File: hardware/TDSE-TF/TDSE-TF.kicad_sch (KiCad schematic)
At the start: 27 parts, among them J1 Sensor nivel de agua, J10 CN10, J2 Tira LED, J3 +5VCC entrada, J5 Bomba, J6 Sensor nivel de luz, J7 CN7, J8 Sensor humedad de suelo, J9 Conector LCD16x02, Q1 IRLZ44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

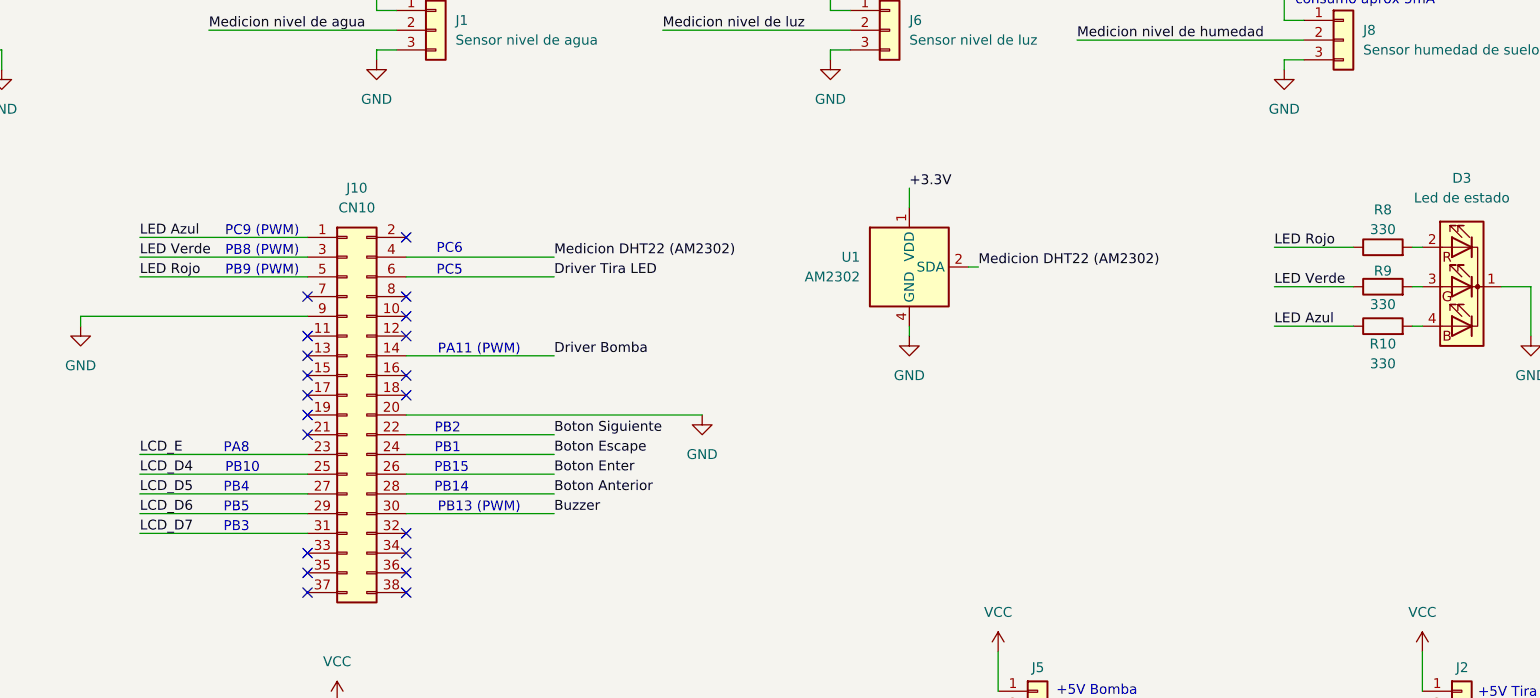
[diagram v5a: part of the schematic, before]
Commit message: PCB final Rev 3
Mejorados detalles del PCB y serigrafía
Añadida opcion de agregar un pullup para el dht22
Modificado el .ioc
Creado task_state_led.h (no terminado)
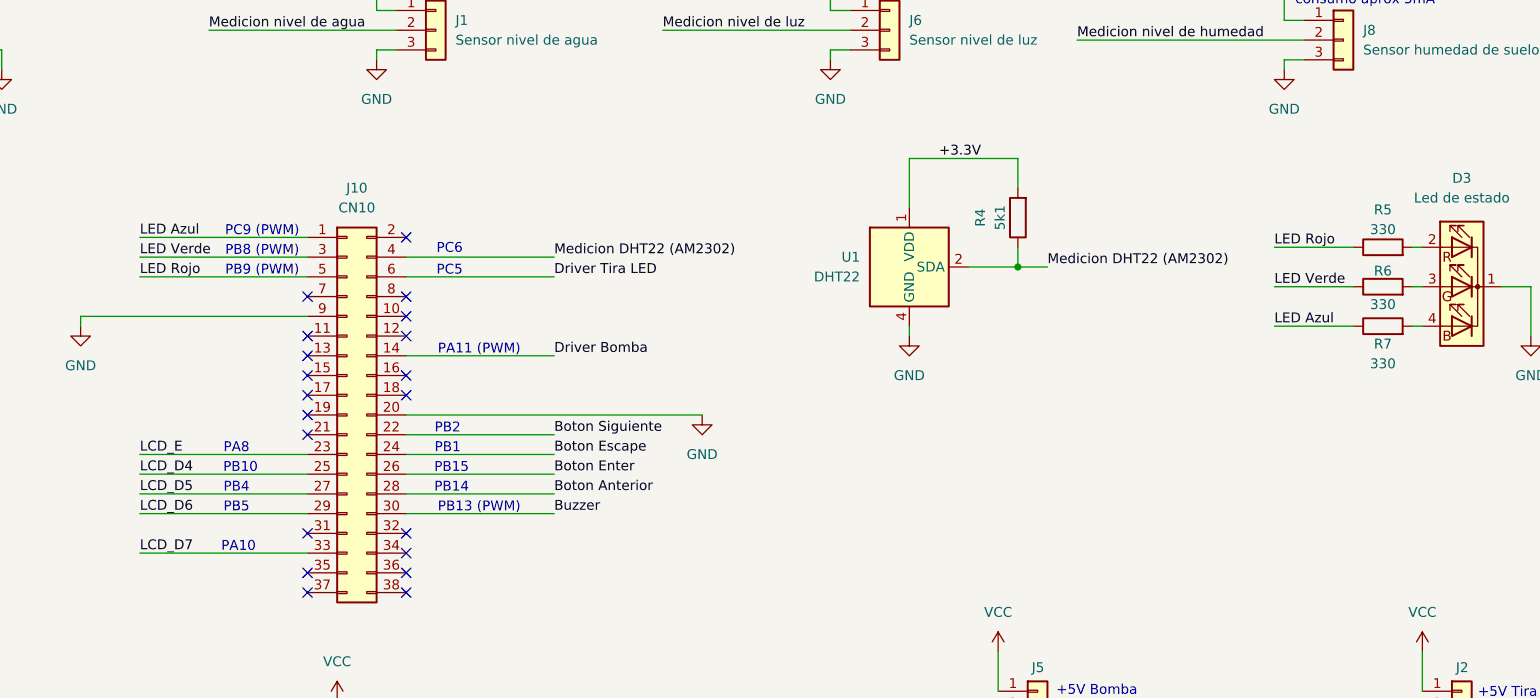
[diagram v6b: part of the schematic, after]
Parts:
- added R4: 5k1, Resistor_THT:R_Axial_DIN0207_L6.3mm_D2.5mm_P7.62mm_Horizontal, symbol Device:R
- U1: value AM2302 -> DHT22
- renumbered R8 to R5, R9 to R6, R10 to R7
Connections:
- net +3.3V: now also R4.2
- net LCD_D7: now also J10.33 (Pin_33); no longer J10.31 (Pin_31)
- net Medicion DHT22 (AM2302): now also R4.1
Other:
- note added: "PA10"
- note removed: "PB3"
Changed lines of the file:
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@@
 		)
 	)
-	(text "PB3"
+	(text "PA10"
 		(exclude_from_sim no)
-		(at 108.966 93.218 0)
+		(at 109.22 95.758 0)
 		(effects
 			(font
@@
 	(text "PB10"
 		(exclude_from_sim no)
-		(at 109.728 85.598 0)
+		(at 109.474 85.598 0)
 		(effects
 			(font
@@
 	)
 	(junction
+		(at 209.55 59.69)
+		(diameter 0)
+		(color 0 0 0 0)
+	)
+	(junction
 		(at 247.65 137.16)
 		(diameter 0)
@@
 	)
 	(no_connect
-		(at 118.11 96.52)
+		(at 118.11 93.98)
 	)
 	(no_connect
@@
 	(wire
 		(pts
+			(xy 209.55 45.72) (xy 195.58 45.72)
+		)
+		(stroke
+			(width 0)
+			(type default)
+		)
+	)
+	(wire
+		(pts
 			(xy 96.52 58.42) (xy 118.11 58.42)
 		)
@@
 	(wire
 		(pts
+			(xy 209.55 57.15) (xy 209.55 59.69)
+		)
+		(stroke
+			(width 0)
+			(type default)
+		)
+	)
+	(wire
+		(pts
 			(xy 191.77 137.16) (xy 191.77 139.7)
 		)
@@
 	(wire
 		(pts
-			(xy 203.2 59.69) (xy 204.47 59.69)
+			(xy 203.2 59.69) (xy 209.55 59.69)
 		)
 		(stroke
@@
 	(wire
 		(pts
+			(xy 209.55 49.53) (xy 209.55 45.72)
+		)
+		(stroke
+			(width 0)
+			(type default)
+		)
+	)
+	(wire
+		(pts
 			(xy 93.98 149.86) (xy 93.98 152.4)
 		)
@@
 	(wire
 		(pts
+			(xy 209.55 59.69) (xy 213.36 59.69)
+		)
+		(stroke
+			(width 0)
+			(type default)
+		)
+	)
+	(wire
+		(pts
 			(xy 137.16 151.13) (xy 146.05 151.13)
 		)
@@
 	(wire
 		(pts
+			(xy 195.58 45.72) (xy 195.58 52.07)
+		)
+		(stroke
+			(width 0)
+			(type default)
+		)
+	)
+	(wire
+		(pts
 			(xy 62.23 181.61) (xy 83.82 181.61)
 		)
@@
 	(wire
 		(pts
-			(xy 195.58 49.53) (xy 195.58 52.07)
-		)
-		(stroke
-			(width 0)
-			(type default)
-		)
-	)
-	(wire
-		(pts
 			(xy 163.83 29.21) (xy 187.96 29.21)
 		)
@@
 	(wire
 		(pts
-			(xy 96.52 93.98) (xy 118.11 93.98)
+			(xy 96.52 96.52) (xy 118.11 96.52)
 		)
 		(stroke
@@
 	)
 	(label "Medicion DHT22 (AM2302)"
-		(at 204.47 59.69 0)
+		(at 213.36 59.69 0)
 		(effects
 			(font
@@
 	)
 	(label "+3.3V"
-		(at 195.58 49.53 0)
+		(at 199.39 45.72 0)
 		(effects
 			(font
@@
 	)
 	(label "LCD_D7"
-		(at 96.52 93.98 0)
+		(at 96.52 96.52 0)
 		(effects
 			(font
@@
 	)
 	(symbol
+		(lib_id "Device:R")
+		(at 209.55 53.34 180)
+		(unit 1)
+		(body_style 1)
+		(exclude_from_sim no)
+		(in_bom yes)
+		(on_board yes)
+		(in_pos_files yes)
+		(dnp no)
+		(property "Reference" "R4"
+			(at 204.724 53.34 90)
+			(show_name no)
+			(do_not_autoplace no)
+			(effects
+				(font
+					(size 1.27 1.27)
+				)
+			)
+		)
+		(property "Value" "5k1"
+			(at 207.264 53.34 90)
+			(show_name no)
+			(do_not_autoplace no)
+			(effects
+				(font
+					(size 1.27 1.27)
+				)
+			)
+		)
+		(property "Footprint" "Resistor_THT:R_Axial_DIN0207_L6.3mm_D2.5mm_P7.62mm_Horizontal"
+			(at 211.328 53.34 90)
+			(hide yes)
+			(show_name no)
+			(do_not_autoplace no)
+			(effects
+				(font
+					(size 1.27 1.27)
+				)
+			)
+		)
+		(property "Datasheet" ""
+			(at 209.55 53.34 0)
+			(hide yes)
+			(show_name no)
+			(do_not_autoplace no)
+			(effects
+				(font
+					(size 1.27 1.27)
+				)
+			)
+		)
+		(property "Description" "Resistor"
+			(at 209.55 53.34 0)
+			(hide yes)
+			(show_name no)
+			(do_not_autoplace no)
+			(effects
+				(font
+					(size 1.27 1.27)
+				)
+			)
+		)
+		(pin "2"
+		)
+		(pin "1"
+		)
+		(instances
+			(project "TDSE-TF"
+				(path "/f326f9a1-cd10-4b99-adfe-c3556115ef97"
+					(reference "R4")
+					(unit 1)
+				)
+			)
+		)
+	)
+	(symbol
 		(lib_id "Connector_Generic:Conn_02x19_Odd_Even")
 		(at 34.29 78.74 0)
@@
 		(in_pos_files yes)
 		(dnp no)
-		(property "Reference" "R8"
+		(property "Reference" "R5"
 			(at 256.54 52.324 90)
 			(show_name no)
@@
 			(project "TDSE-TF"
 				(path "/f326f9a1-cd10-4b99-adfe-c3556115ef97"
-					(reference "R8")
+					(reference "R5")
 					(unit 1)
 				)
@@
 		(in_pos_files yes)
 		(dnp no)
-		(property "Reference" "R9"
+		(property "Reference" "R6"
 			(at 256.54 60.198 90)
 			(show_name no)
@@
 			(project "TDSE-TF"
 				(path "/f326f9a1-cd10-4b99-adfe-c3556115ef97"
-					(reference "R9")
+					(reference "R6")
 					(unit 1)
 				)
@@
 		(in_pos_files yes)
 		(dnp no)
-		(property "Reference" "R10"
+		(property "Reference" "R7"
 			(at 256.54 69.596 90)
 			(show_name no)
@@
 			(project "TDSE-TF"
 				(path "/f326f9a1-cd10-4b99-adfe-c3556115ef97"
-					(reference "R10")
+					(reference "R7")
 					(unit 1)
 				)
@@
 			)
 		)
-		(property "Value" "AM2302"
+		(property "Value" "DHT22"
 			(at 189.23 60.9599 0)
 			(show_name no)

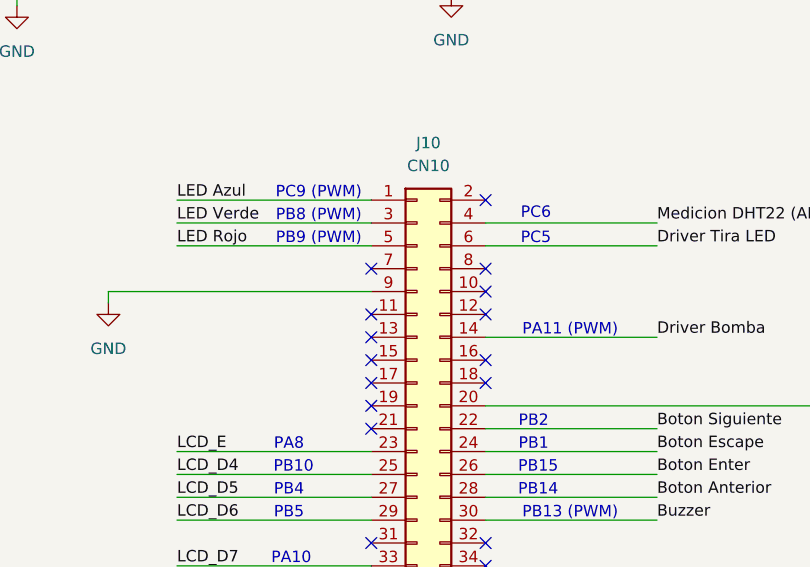
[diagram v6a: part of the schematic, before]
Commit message: PCB final Rev 4 y agregado led de estado RGB
Agregó la lógica de LED RGB de estado con PWM
Se mejoró el PCB y se incorporaron fichas de conexión mejores para alimentacion y cargas
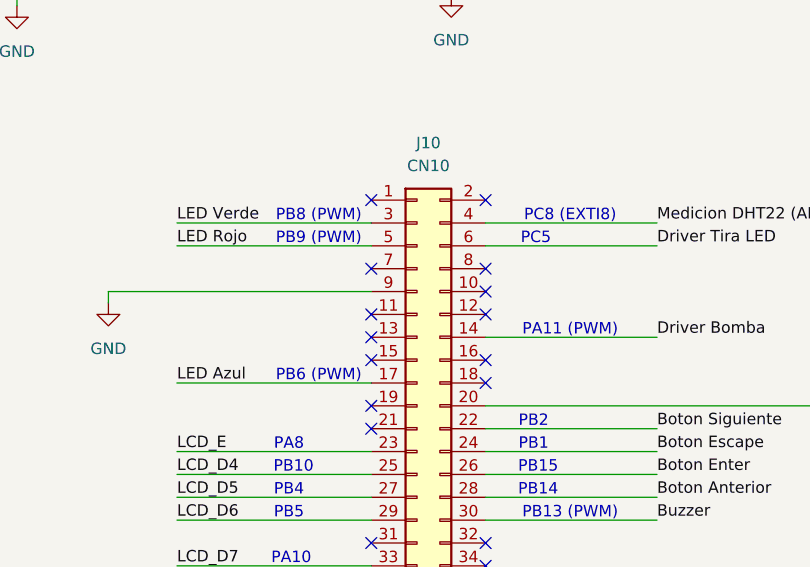
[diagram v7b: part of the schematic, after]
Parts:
- J2, J3, J5: footprint Connector_PinHeader_2.54mm:PinHeader_1x02_P2.54mm_Vertical -> Connector_JST:JST_EH_B2B-EH-A_1x02_P2.50mm_Vertical
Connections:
- net LED Azul: now also J10.17 (Pin_17); no longer J10.1 (Pin_1)
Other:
- note added: "PB6 (PWM)"
- note added: "PC8 (EXTI8)"
- note removed: "PC6"
- note removed: "PC9 (PWM)"
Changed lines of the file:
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@@
 		)
 	)
-	(text "PC9 (PWM)"
+	(text "PB6 (PWM)"
 		(exclude_from_sim no)
-		(at 112.268 55.118 0)
+		(at 112.268 75.438 0)
 		(effects
 			(font
@@
 		)
 	)
-	(text "PC6\n"
+	(text "PC8 (EXTI8)\n"
 		(exclude_from_sim no)
-		(at 136.398 57.404 0)
+		(at 140.208 57.658 0)
 		(effects
 			(font
@@
 	)
 	(no_connect
-		(at 118.11 76.2)
+		(at 118.11 55.88)
 	)
 	(no_connect
@@
 	(wire
 		(pts
-			(xy 96.52 55.88) (xy 118.11 55.88)
+			(xy 96.52 76.2) (xy 118.11 76.2)
 		)
 		(stroke
@@
 	)
 	(label "LED Azul"
-		(at 96.52 55.88 0)
+		(at 96.52 76.2 0)
 		(effects
 			(font
@@
 			)
 		)
-		(property "Footprint" "Connector_PinHeader_2.54mm:PinHeader_1x02_P2.54mm_Vertical"
+		(property "Footprint" "Connector_JST:JST_EH_B2B-EH-A_1x02_P2.50mm_Vertical"
 			(at 212.09 114.3 0)
 			(hide yes)
@@
 			)
 		)
-		(property "Footprint" "Connector_PinHeader_2.54mm:PinHeader_1x02_P2.54mm_Vertical"
+		(property "Footprint" "Connector_JST:JST_EH_B2B-EH-A_1x02_P2.50mm_Vertical"
 			(at 38.1 33.02 0)
 			(hide yes)
@@
 			)
 		)
-		(property "Footprint" "Connector_PinHeader_2.54mm:PinHeader_1x02_P2.54mm_Vertical"
+		(property "Footprint" "Connector_JST:JST_EH_B2B-EH-A_1x02_P2.50mm_Vertical"
 			(at 266.7 114.3 0)
 			(hide yes)

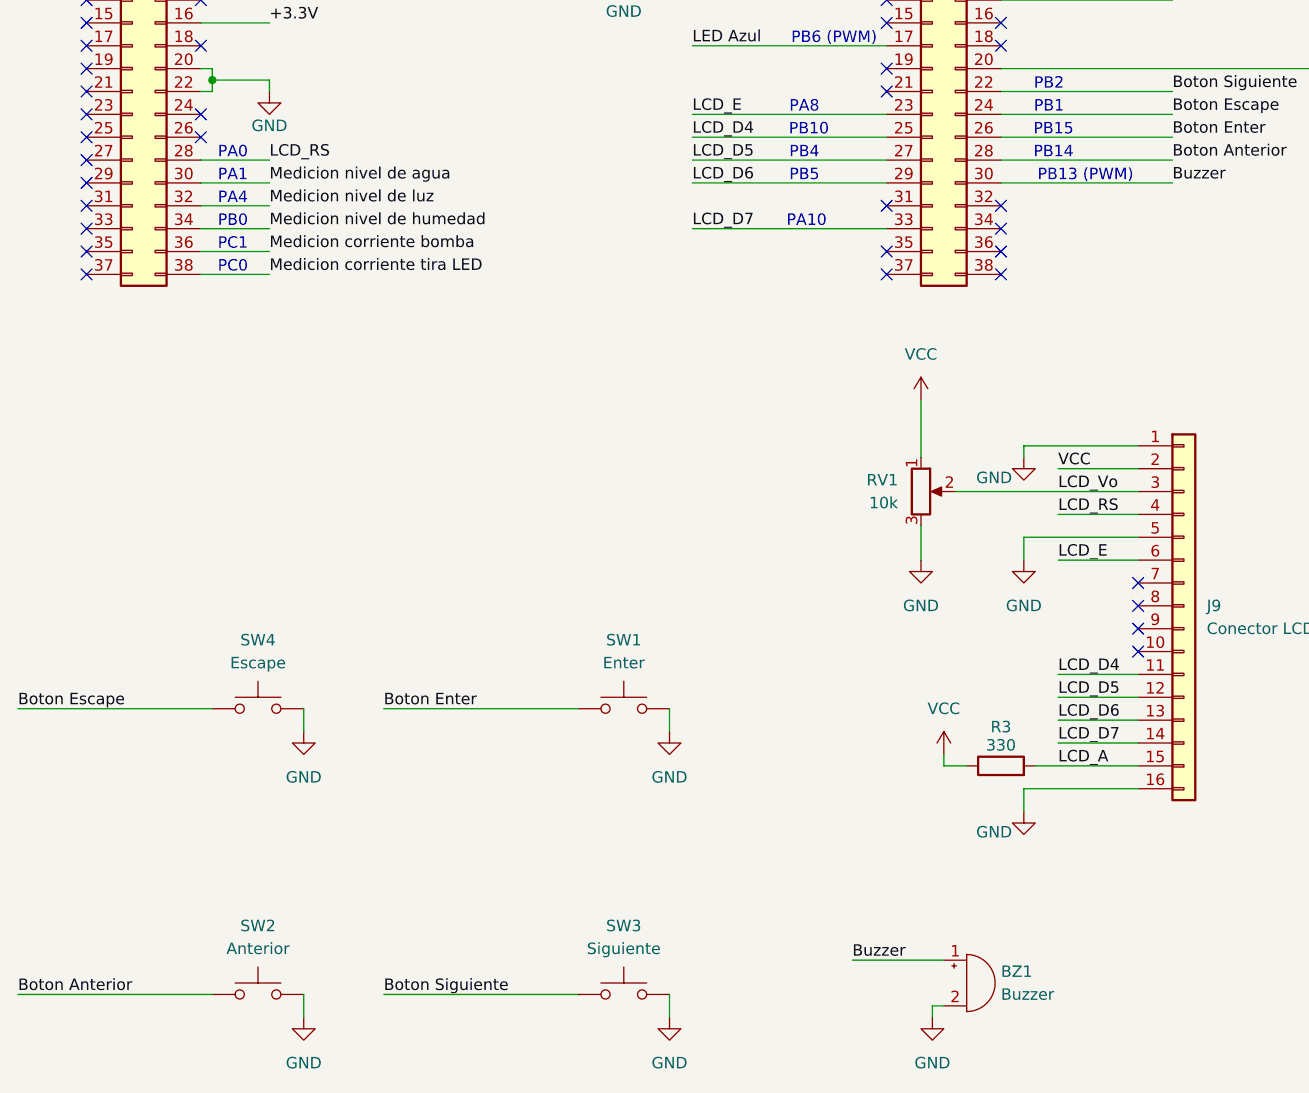
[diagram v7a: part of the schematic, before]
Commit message: PCB final Rev 5 y buzzer
Se añadió la funcionalidad de buzzer al código
Se añadió un transistor como driver par el buzzer
Se actualizó el PCB
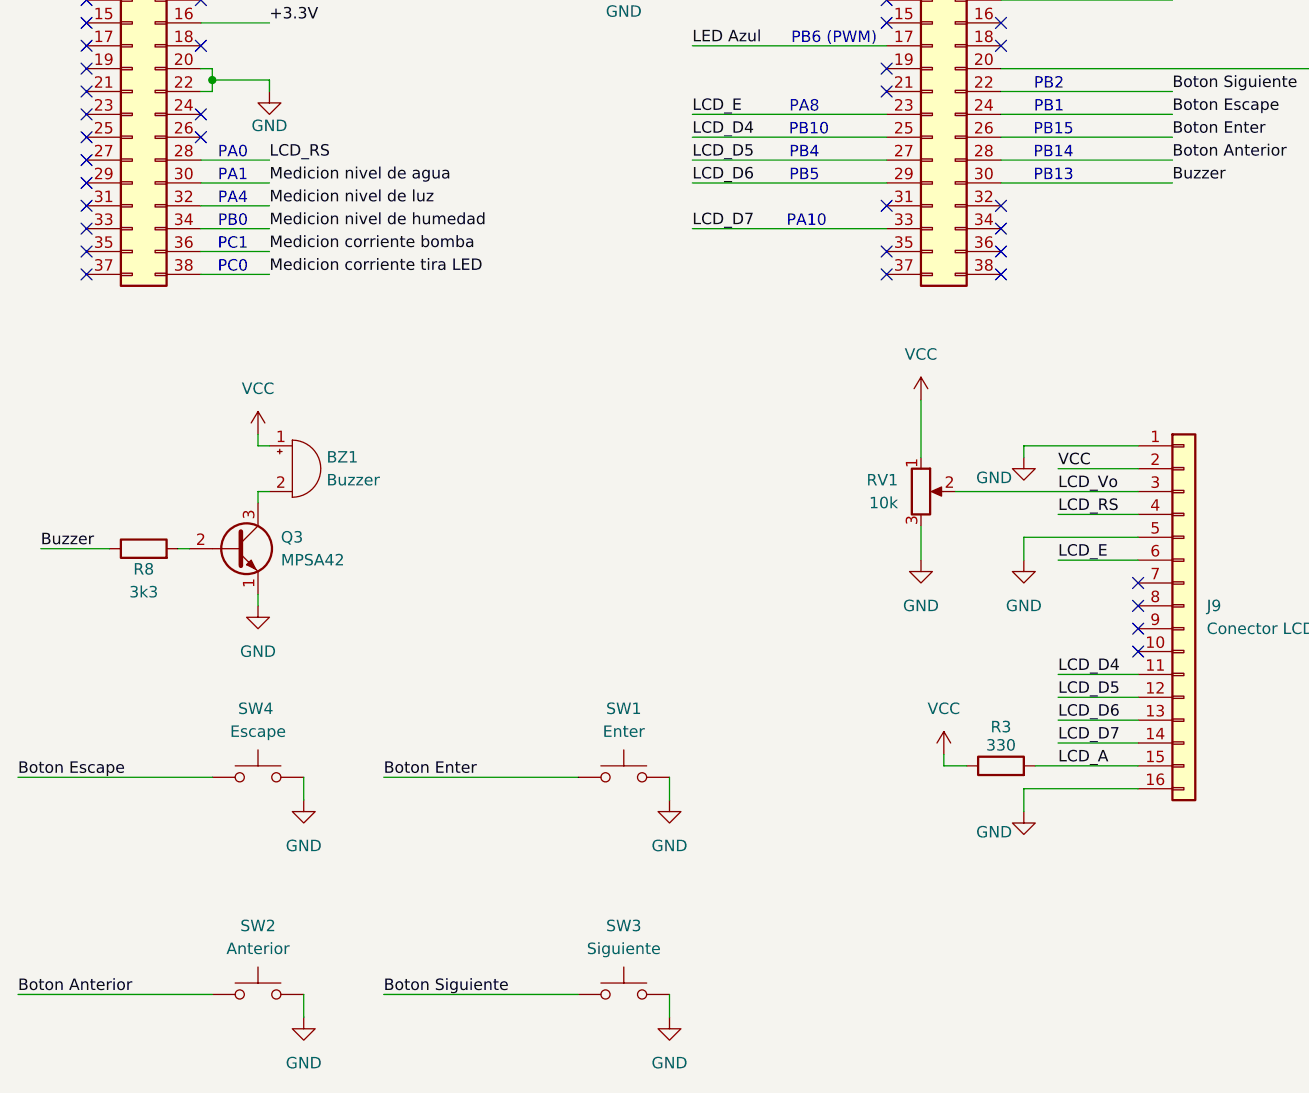
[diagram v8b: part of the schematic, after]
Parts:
- added Q3: MPSA42, Package_TO_SOT_THT:TO-92_Inline, symbol Transistor_BJT:MPSA42
- added R8: 3k3, Resistor_THT:R_Axial_DIN0207_L6.3mm_D2.5mm_P7.62mm_Horizontal, symbol Device:R
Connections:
- net Buzzer: now also R8.1; no longer BZ1.1 (+)
- net GND: now also Q3.1 (E); no longer BZ1.2 (-)
- net VCC: now also BZ1.1 (+)
- new net: Q3.2 (B), R8.2
- new net: BZ1.2 (-), Q3.3 (C)
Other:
- note added: "PB13"
- note removed: "PB13 (PWM)"
- moved on the sheet: BZ1, SW1, SW4
